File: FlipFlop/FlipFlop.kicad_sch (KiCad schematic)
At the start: 14 parts, among them SW1 SW_Push, SW2 SW_Push, U1 74HC74, U2 74HC74

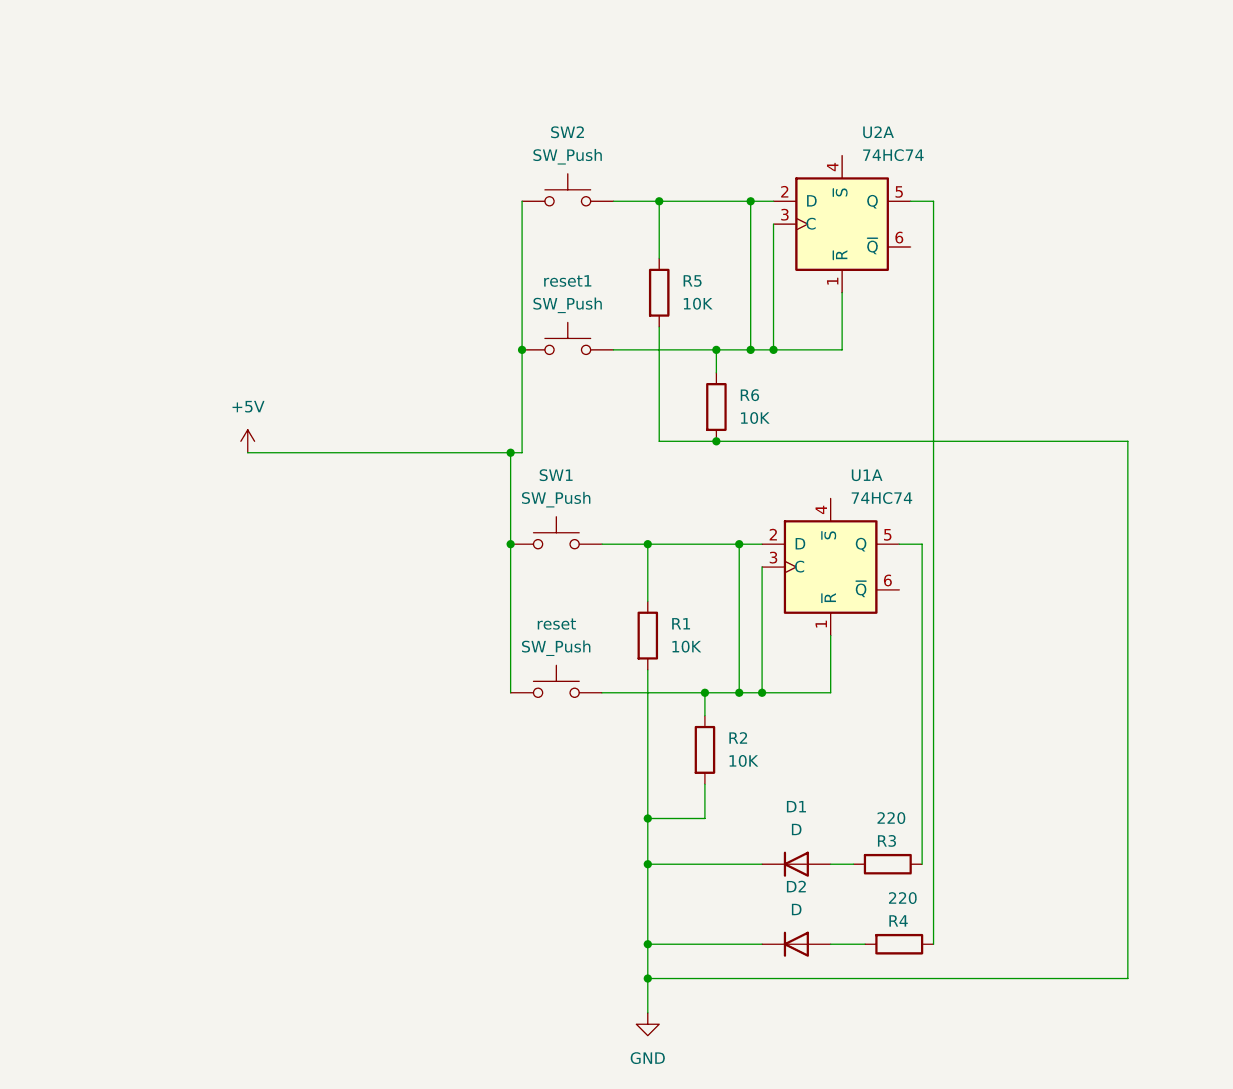
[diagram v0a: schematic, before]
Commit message: Verified FlipFlop reset did not need a clock signal
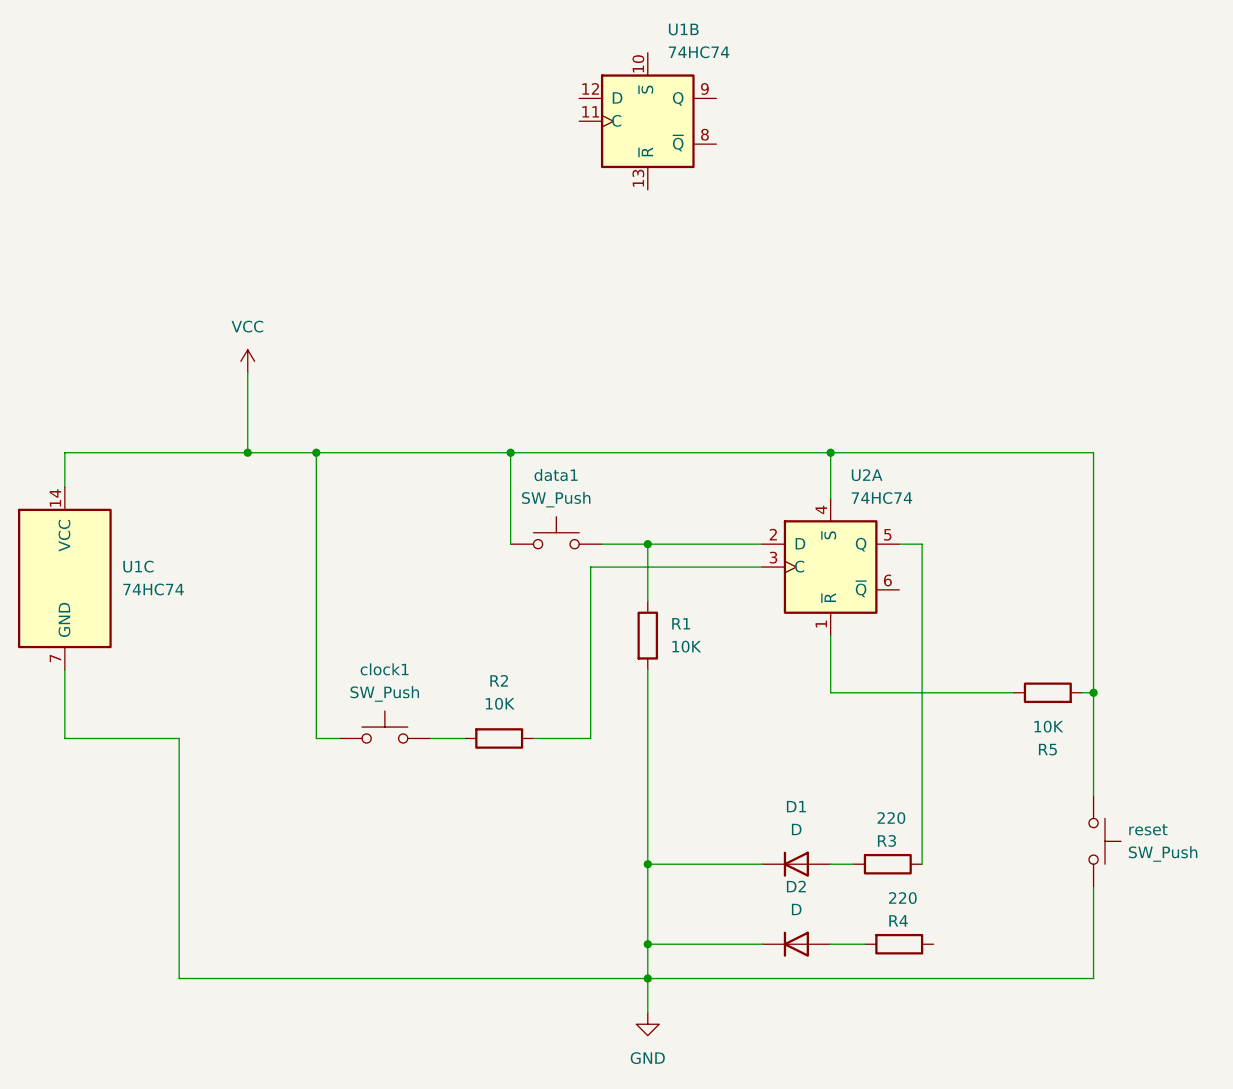
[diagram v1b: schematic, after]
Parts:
- removed R6: 10K, symbol Device:R
- removed SW2, reset1: SW_Push, Button_Switch_THT:SW_Tactile_Straight_KSA0Axx1LFTR, symbol Switch:SW_Push
- removed U1: 74HC74, Package_DIP:DIP-14_W7.62mm_Socket, symbol 74xx:74HC74
- added U1: 74HC74, Package_DIP:DIP-14_W7.62mm_Socket, symbol 74xx:74HC74
- added reset: SW_Push, Button_Switch_THT:SW_Tactile_Straight_KSA0Axx1LFTR, symbol Switch:SW_Push
- renumbered reset to clock1, SW1 to data1
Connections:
- net +5V is gone; now on net VCC: clock1.1, data1.1
- net GND: now also U1.7 (GND), reset.2; no longer R2.2, R5.2
- net at R5.1, U2.1 (~{R}): no longer U2.2 (D), U2.3 (C)
- net at R3.1: now also U2.5 (Q)
- net VCC: now reaches U2.4 (~{S})
- net VCC: now also R5.2, U1.14 (VCC), reset.1
- net at R4.1: no longer U2.5 (Q)
- net at R1.1, data1.2: now also U2.2 (D); no longer R2.1, clock1.2
- new net: R2.2, clock1.2
- new net: R2.1, U2.3 (C)
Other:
- moved on the sheet: R2, clock1
